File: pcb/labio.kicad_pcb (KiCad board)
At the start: 2 copper layers, 152 x 85 mm, 219 parts, among them IC201 dnp-AT24CS32-XHM, J701 JACK_TRRS_6PINS, P201 CONN_02X20, P301 CONN_01X04, P302 CONN_01X04, P303 CONN_01X04, P401 SFV12R-1ST__HLF, P601 CONN_01X02, P602 CONN_01X02, P603 CONN_01X04, P604 CONN_01X02, P605 CONN_01X03, P606 CONN_01X03, P607 CONN_01X05, P608 CONN_01X05, P701 CONN_01X04, P702 CONN_01X04, P703 CONN_01X04, P704 CONN_01X02, P901 CONN_01X06, Q301 PHOTOTRANSISTOR, Q302 Q_NMOS_GSD, Q303 Q_NMOS_GSD, Q601 Q_NMOS_GSD, Q602 Q_NMOS_GSD, Q603 Q_NMOS_GSD, Q604 Q_NMOS_GSD, Q605 Q_NMOS_GSD, Q606 Q_NMOS_GSD, Q607 Q_NMOS_GSD, Q608 Q_NMOS_GSD, Q609 Q_NMOS_GSD, Q610 Q_NMOS_GSD, Q611 Q_NMOS_GSD, Q612 Q_NMOS_GSD, Q613 Q_NMOS_GSD, SW301 DIP_SWITCH_X04, SW401 DIP_SWITCH_X04, SW501 DIP_SWITCH_X04, SW601 DIP_SWITCH_X04, SW602 DIP_SWITCH_X04, SW603 DIP_SWITCH_X04, SW604 DIP_SWITCH_X04, SW605 ROT_ENC, SW606 DIP_SWITCH_X04, SW701 DIP_SWITCH_X04, SW702 DIP_SWITCH_X04, SW801 SW_PUSH, SW802 SW_PUSH, SW803 SW_PUSH, SW804 SW_PUSH, SW805 SW_PUSH, U201 AP7365_SOT-23-5, U301 ADS1015, U501 LSM303D, U502 BMP280, U503 L3GD20H, U601 L298P_PowerSO20, U701 SPU0410HR5H, U702 WM8750

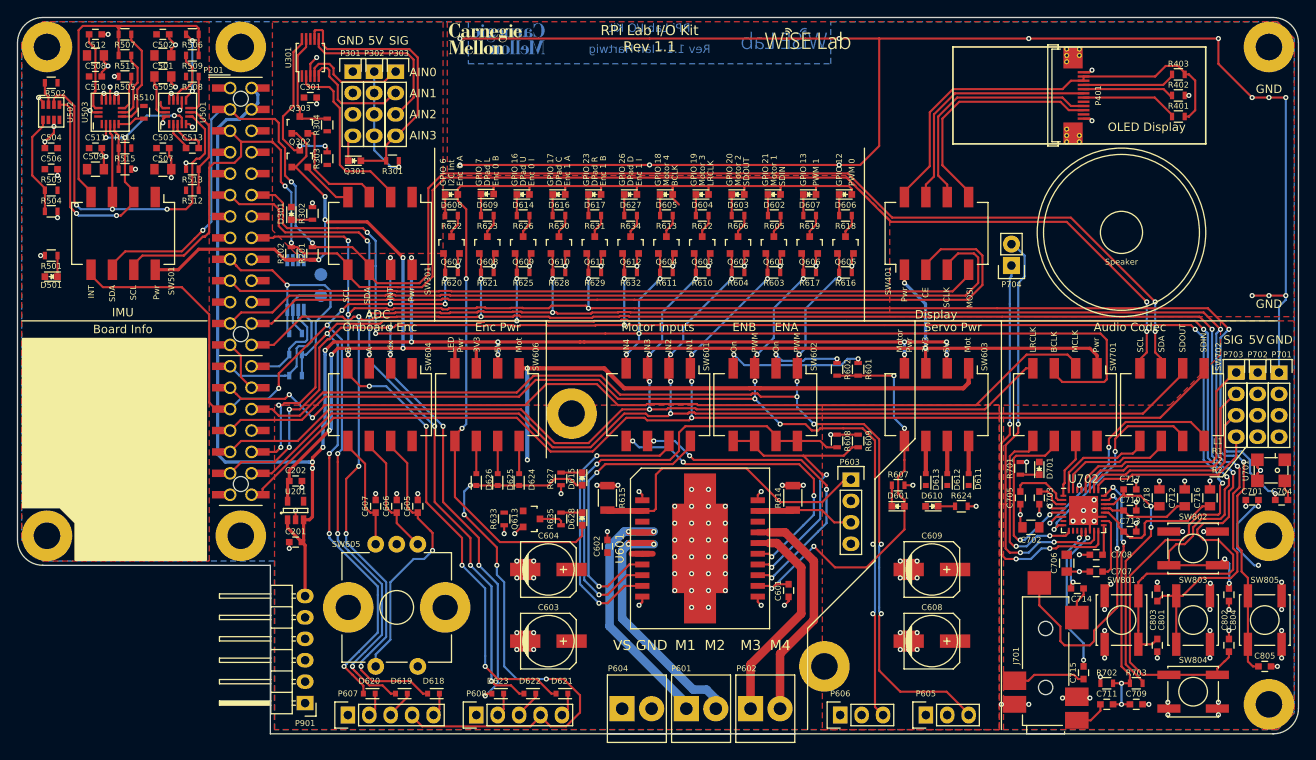
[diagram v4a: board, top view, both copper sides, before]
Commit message: add fuses for connectable headers (adc, encoder, motors, servo, codec). GERBER/BOM UPDATES ONLY
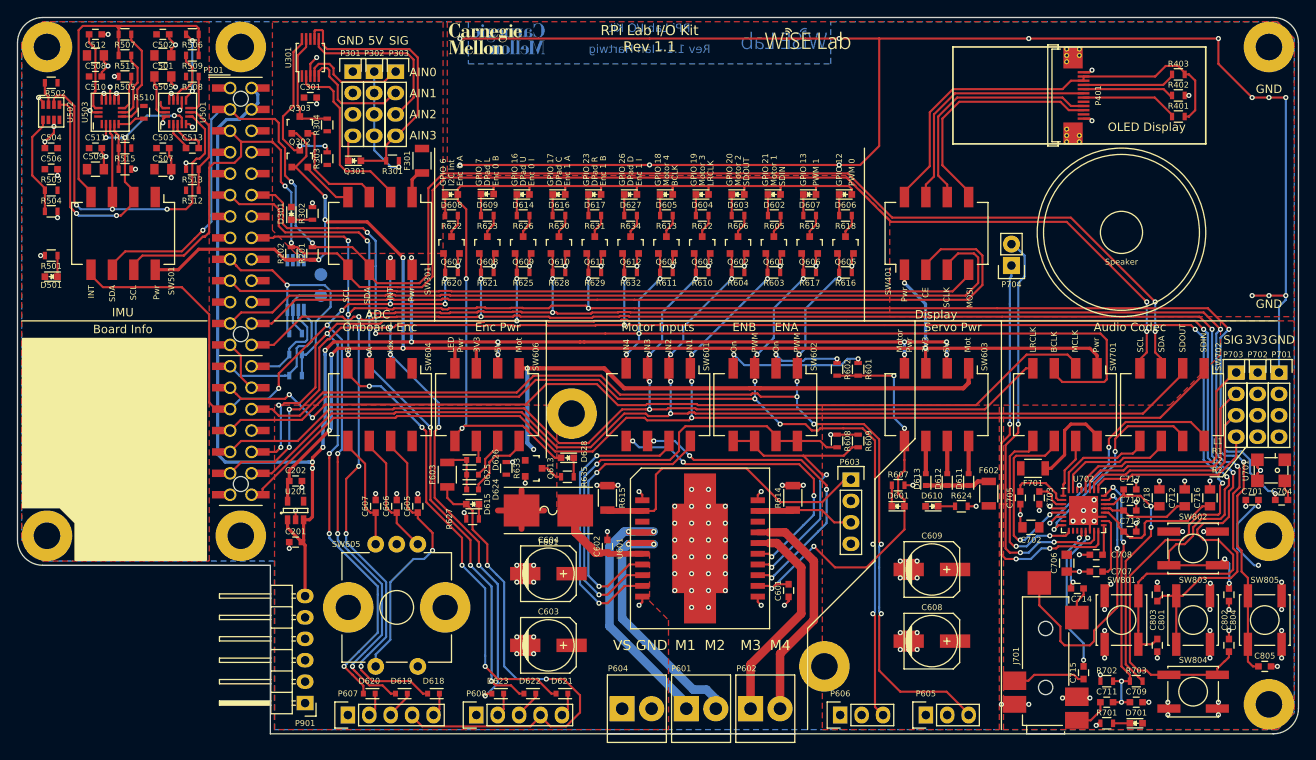
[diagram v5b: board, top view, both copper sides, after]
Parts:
- added F301: F_Small, Resistors_SMD:R_1206, F.Cu at (125.0, 67.0)
- added F601: F_Small, labio-special:OMNI-BLOCK_Fuse_10x5mm_Littelfuse, F.Cu at (140.0, 108.5)
- added F602: F_Small, Resistors_SMD:R_1206, F.Cu at (192.2, 106.5)
- added F603: F_Small, Resistors_SMD:R_1206, F.Cu at (128.0, 104.2)
- added F701: F_Small, Resistors_SMD:R_1206, F.Cu at (197.5, 103.5)
- moved D701 32.4 mm to (209.8, 133.8), turned to 0 degrees
- moved R701 31.9 mm to (206.2, 133.8), turned to 0 degrees
- moved D615 13.3 mm to (131.0, 107.8), turned to 180 degrees
- moved R627 11.5 mm to (131.0, 109.5), turned to 180 degrees
- moved D628 7.46 mm to (142.2, 102.2), turned to 180 degrees
- moved Q613 6.01 mm to (138.2, 103.5)
- moved R633 6.01 mm to (135.0, 103.5), turned to 90 degrees
- moved D624 5.65 mm to (131.0, 106.0), turned to 180 degrees
- moved R635 5.06 mm to (142.2, 104.5), turned to 180 degrees
- moved D625 3.04 mm to (131.0, 104.2), turned to 180 degrees
- moved D626 2.37 mm to (131.0, 102.5), turned to 180 degrees
- moved C603 0.50 mm to (140.0, 124.5)
- moved C604 0.50 mm to (140.0, 116.0)
- moved C709 0.25 mm to (209.8, 131.2)
- moved C711 0.25 mm to (206.2, 131.2)
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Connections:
- C602 pad 1: /labio-dio/VS_MOTOR -> /labio-dio/VS_MOTOR_F
- D611 pad 1: /labio-dio/VDD_SERVO -> /labio-dio/VDD_SERVO_F
- D612 pad 1: /labio-dio/VDD_SERVO -> /labio-dio/VDD_SERVO_F
- D613 pad 1: /labio-dio/VDD_SERVO -> /labio-dio/VDD_SERVO_F
- D624 pad 1: /labio-dio/VDD_ENC -> /labio-dio/VDD_ENC_F
- D625 pad 1: /labio-dio/VDD_ENC -> /labio-dio/VDD_ENC_F
- D626 pad 1: /labio-dio/VDD_ENC -> /labio-dio/VDD_ENC_F
- H1001 pad 1: Net-(H1001-Pad1) -> (no net)
- H1002 pad 1: Net-(H1002-Pad1) -> (no net)
- H1003 pad 1: Net-(H1003-Pad1) -> (no net)
- H1004 pad 1: Net-(H1004-Pad1) -> (no net)
- H1005 pad 1: Net-(H1005-Pad1) -> (no net)
- H1006 pad 1: Net-(H1006-Pad1) -> (no net)
- H1007 pad 1: Net-(H1007-Pad1) -> (no net)
- H1008 pad 1: Net-(H1008-Pad1) -> (no net)
- H1009 pad 1: Net-(H1009-Pad1) -> (no net)
- J701 pad 6: Net-(J701-Pad6) -> (no net)
- P401 pad 11: Net-(P401-Pad11) -> (no net)
- P401 pad 8: Net-(P401-Pad8) -> (no net)
- P901 pad 5: Net-(P901-Pad5) -> (no net)
- SW301 pad 1: /labio-adc/VDD5V_J -> /labio-adc/VDD_J_F
- SW604 pad 1: Net-(SW604-Pad1) -> (no net)
- SW604 pad 8: Net-(SW604-Pad8) -> (no net)
- SW701 pad 8: /labio-audio/VDD3V3_J -> /labio-audio/VDD3V3_J_F
- U601 pad 6: /labio-dio/VS_MOTOR -> /labio-dio/VS_MOTOR_F
- U702 pad 10: Net-(U702-Pad10) -> (no net)
- U702 pad 11: Net-(U702-Pad11) -> (no net)
- U702 pad 7: Net-(U702-Pad7) -> (no net)
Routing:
- net /labio-dio/VDD_LED: track 115.5 -> 102.1 mm
- net /labio-dio/VDD_ENC: track 72.5 -> 59.8 mm, vias 4 -> 2
- net /labio-dio/VS_MOTOR_F: track 0.00 -> 11.6 mm
- net /labio-audio/VDD3V3_J_F: track 0.00 -> 11.2 mm
- net /labio-dio/VDD_SERVO_F: track 0.00 -> 7.66 mm
- net /labio-dio/VS_MOTOR: track 69.7 -> 76.4 mm
- net /labio-dio/VDD_ENC_F: track 0.00 -> 5.92 mm
- net Net-(D624-Pad2): track 3.88 -> 8.74 mm
- net /labio-adc/VDD_J_F: track 0.00 -> 3.58 mm
- net Net-(J701-Pad6): track 3.25 -> 0.00 mm, vias 2 -> 0
- net (no net): track 0.00 -> 3.25 mm, vias 0 -> 2
- net GND: track 408.9 -> 407.4 mm
- net Net-(D626-Pad2): track 3.88 -> 2.36 mm
- net Net-(D625-Pad2): track 3.88 -> 4.95 mm
- net Net-(D615-Pad1): track 2.50 -> 1.75 mm

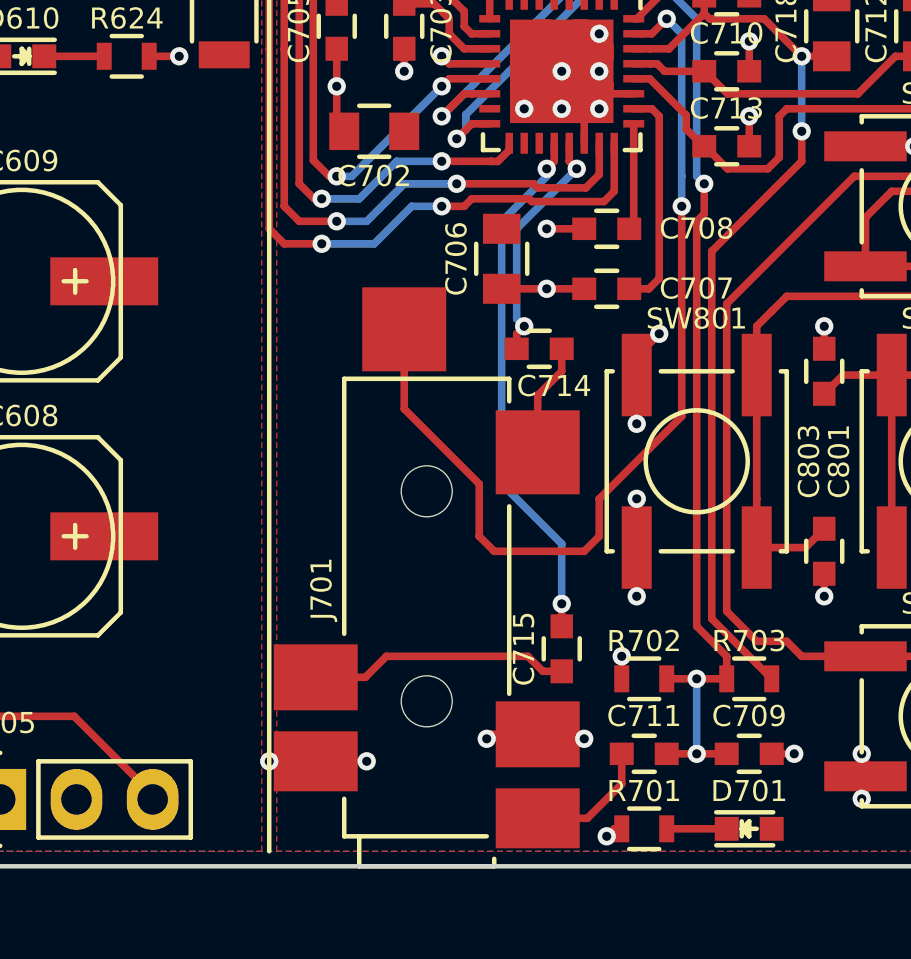
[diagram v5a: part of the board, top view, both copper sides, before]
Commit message: fix codec/mic/trrs bias circuit
* trrs (headset) mic bias was flipped (in vs out) from datasheet
* trrs l/r decoupling caps changed back to 220uF per datasheet and re-layout for 1210 ceramic
* mems mic decoupling changed to 1uF for consistency
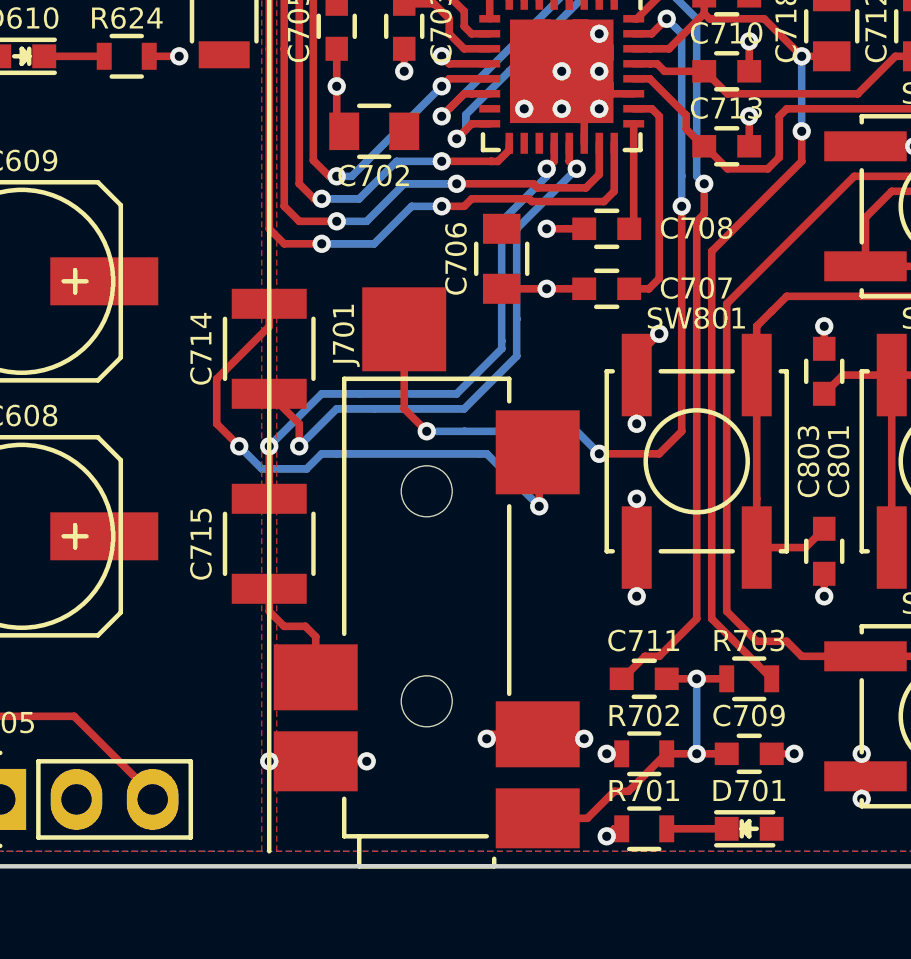
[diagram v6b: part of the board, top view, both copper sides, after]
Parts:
- C704: value 2.2uF -> 1uF
- C714, C715: value 220pF -> 220uF; footprint Capacitors_SMD:C_0603 -> Capacitors_SMD:C_1210
- moved C715 10.4 mm to (193.8, 124.2)
- moved C714 9.00 mm to (193.8, 117.8), turned to 270 degrees
- moved C711 2.50 mm to (206.2, 128.8), turned to 0 degrees
- moved R702 2.50 mm to (206.2, 131.2)
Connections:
- C709 pad 1: /labio-audio/TRRS_MIC_BIAS -> /labio-audio/TRRS_MIC_BIASED
- C711 pad 1: /labio-audio/TRRS_MIC_BIAS -> /labio-audio/TRRS_MIC
- C711 pad 2: /labio-audio/TRRS_MIC -> /labio-audio/TRRS_MIC_BIASED
- J701 pad 1: /labio-audio/TRRS_MIC -> /labio-audio/TRRS_MIC_BIASED
- R702 pad 1: /labio-audio/TRRS_MIC_BIAS -> /labio-audio/TRRS_MIC_BIASED
- R703 pad 2: /labio-audio/TRRS_MIC_BIAS -> /labio-audio/TRRS_MIC_BIASED
- U702 pad 24: /labio-audio/TRRS_MIC_BIAS -> /labio-audio/TRRS_MIC
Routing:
- net /labio-audio/TRRS_MIC_BIAS: track 32.0 -> 0.00 mm, vias 4 -> 0
- net /labio-audio/TRRS_MIC: track 4.28 -> 26.5 mm, vias 0 -> 2
- net /labio-audio/TRRS_L: track 3.78 -> 18.8 mm, vias 0 -> 2
- net /labio-audio/TRRS_MIC_BIASED: track 0.00 -> 11.7 mm, vias 0 -> 2
- net /labio-audio/TRRS_L_C: track 7.99 -> 18.7 mm
- net /labio-audio/TRRS_R: track 8.70 -> 4.01 mm
- net /labio-audio/TRRS_HPDETECT: track 31.3 -> 28.1 mm, vias 2 -> 4
- net /labio-audio/TRRS_R_C: track 17.7 -> 18.4 mm

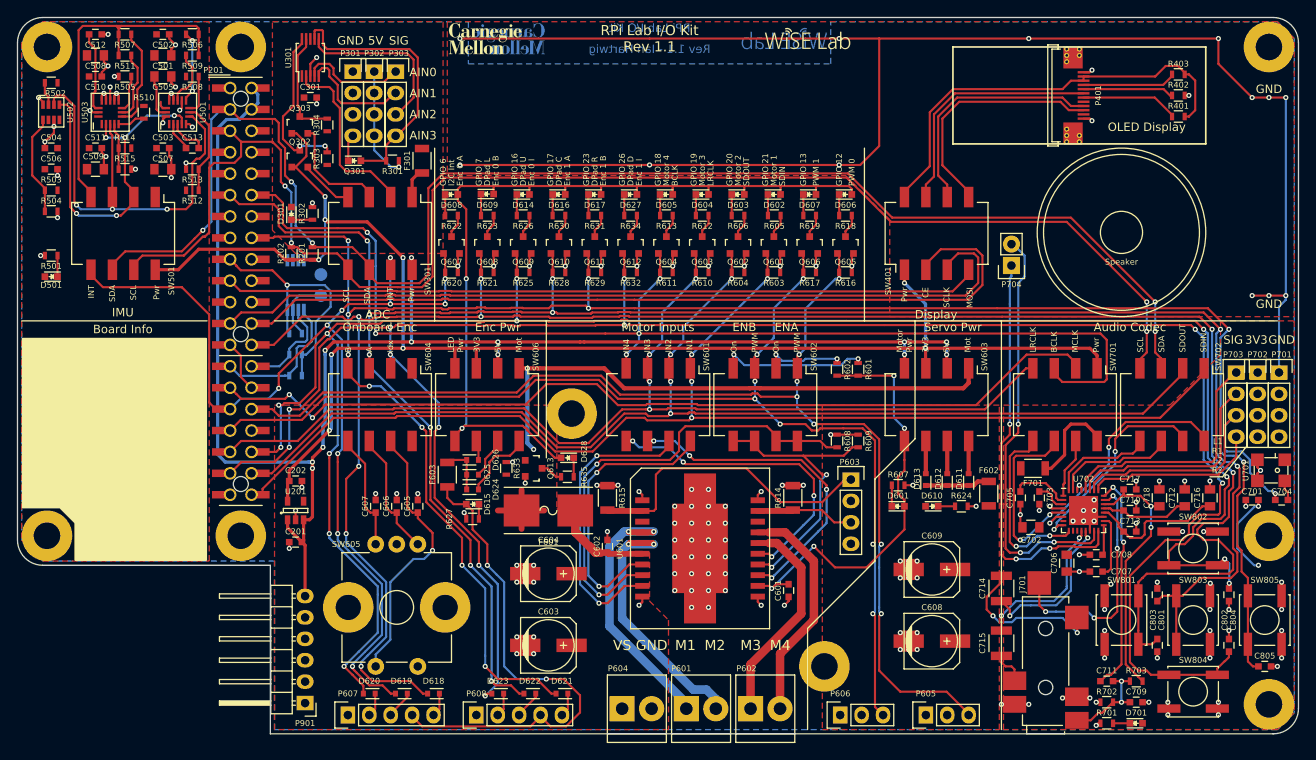
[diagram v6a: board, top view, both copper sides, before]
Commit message: Fix ADC reading mic, possible backpowering, encoder pull downs, vias in footprint:
* Mic needs on-board path to ADC. Add proper bias and amp. Connect to ADC or codec with switches.
* Mic footprint (U701) flipped. Redraw footprint and adjust routing.
* Remove power from dip switches and replace with fuses. Turning power off to a block could result in backpower from driven IO lines.
* Remove/adjust pull downs on LEDs for encoder/dpad lines.
* Move vias out of display connector (P401) footprint.
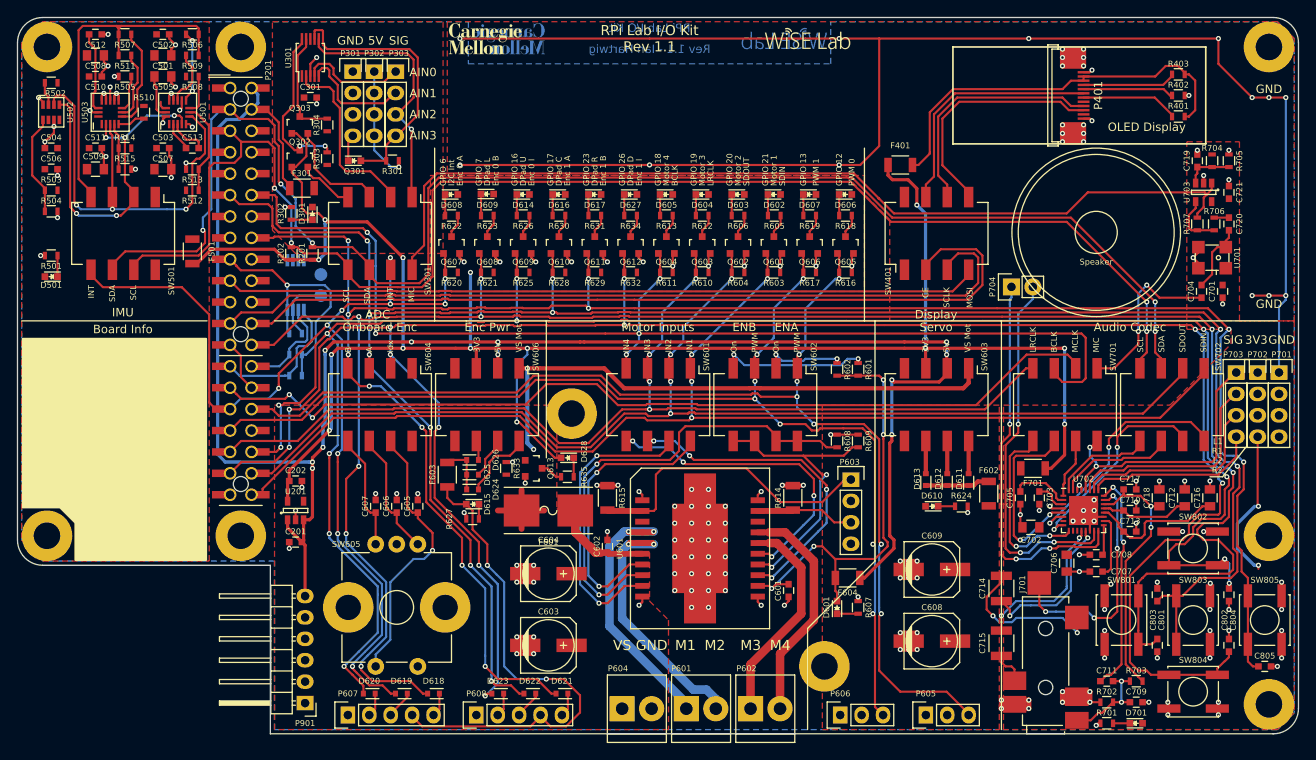
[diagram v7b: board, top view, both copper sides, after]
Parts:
- added C719: 1uF, Capacitors_SMD:C_0603, F.Cu at (217.0, 67.0)
- added C720: 1uF, Capacitors_SMD:C_0603, F.Cu at (220.8, 74.5)
- added C721: 0.1uF, Capacitors_SMD:C_0603, F.Cu at (220.8, 70.8)
- added F401: F_Small, Resistors_SMD:R_1206, F.Cu at (181.8, 67.5)
- added F501: F_Small, Resistors_SMD:R_1206, F.Cu at (97.8, 77.8)
- added F604: F_Small, Resistors_SMD:R_1206, F.Cu at (175.5, 116.5)
- added R704: 10k, Resistors_SMD:R_0603, F.Cu at (218.8, 67.0)
- added R705: 10k, Resistors_SMD:R_0603, F.Cu at (220.8, 67.0)
- added R706: 10k, Resistors_SMD:R_0603, F.Cu at (219.0, 74.5)
- added R707: 820k, Resistors_SMD:R_0603, F.Cu at (217.0, 74.5)
- added U703: OPA344_SOT23-5, TO_SOT_Packages_SMD:SOT-23-5, F.Cu at (217.8, 70.8)
- moved C704 26.5 mm to (217.5, 82.5), turned to 90 degrees
- moved U701 26.2 mm to (218.8, 78.5)
- moved C701 25.0 mm to (220.0, 82.5), turned to 90 degrees
- moved R607 15.3 mm to (176.8, 120.0), turned to 90 degrees
- moved F301 14.6 mm to (110.8, 70.2), turned to 180 degrees
- moved D601 14.0 mm to (174.2, 120.0), turned to 90 degrees
- moved P704 2.54 mm to (194.9, 82.0), turned to 90 degrees
- moved D301 2.50 mm to (112.0, 73.2)
- moved R302 2.50 mm to (109.5, 73.2)
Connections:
- net /labio-adc/ACD_AIN0 renamed /labio-adc/ADC_AIN0
- C704 pad 1: /labio-audio/LINPUT2 -> /labio-audio/MEMS_MIC_C
- D602 pad 2: /labio-dio/VDD_LED -> /3V3_EXTRA
- D603 pad 2: /labio-dio/VDD_LED -> /3V3_EXTRA
- D604 pad 2: /labio-dio/VDD_LED -> /3V3_EXTRA
- D605 pad 2: /labio-dio/VDD_LED -> /3V3_EXTRA
- D606 pad 2: /labio-dio/VDD_LED -> /3V3_EXTRA
- D607 pad 2: /labio-dio/VDD_LED -> /3V3_EXTRA
- D608 pad 2: /labio-dio/VDD_LED -> /3V3_EXTRA
- D609 pad 2: /labio-dio/VDD_LED -> /3V3_EXTRA
- D614 pad 2: /labio-dio/VDD_LED -> /3V3_EXTRA
- D616 pad 2: /labio-dio/VDD_LED -> /3V3_EXTRA
- D617 pad 2: /labio-dio/VDD_LED -> /3V3_EXTRA
- D627 pad 2: /labio-dio/VDD_LED -> /3V3_EXTRA
- D628 pad 2: /labio-dio/VDD_LED -> /3V3_EXTRA
- F301 pad 2: /labio-adc/VDD_J_F -> /5V
- F701 pad 1: /labio-audio/VDD3V3_J_F -> /3V3_EXTRA
- P401 pad 2: Net-(P401-Pad2) -> Net-(F401-Pad2)
- P401 pad 3: Net-(P401-Pad2) -> Net-(F401-Pad2)
- R401 pad 2: Net-(P401-Pad2) -> Net-(F401-Pad2)
- R403 pad 2: Net-(P401-Pad2) -> Net-(F401-Pad2)
- R607 pad 1: GND -> Net-(D601-Pad1)
- R607 pad 2: Net-(D601-Pad1) -> GND
- R620 pad 2: GND -> /3V3_EXTRA
- R621 pad 2: GND -> /3V3_EXTRA
- R625 pad 2: GND -> /3V3_EXTRA
- R628 pad 2: GND -> /3V3_EXTRA
- R629 pad 2: GND -> /3V3_EXTRA
- R632 pad 2: GND -> /3V3_EXTRA
- SW301 pad 1: /labio-adc/VDD_J_F -> /labio-adc/ADC_AIN2
- SW301 pad 8: /5V -> MEMS_MIC_TO_ADC
- SW401 pad 1: /3V3_EXTRA -> (no net)
- SW401 pad 8: Net-(P401-Pad2) -> (no net)
- SW501 pad 1: /labio-imu/VDD3V3_J -> (no net)
- SW501 pad 8: /3V3_EXTRA -> (no net)
- SW603 pad 4: /5V -> (no net)
- SW603 pad 5: /labio-dio/VDD_MOT -> (no net)
- SW606 pad 4: /3V3_EXTRA -> (no net)
- SW606 pad 5: /labio-dio/VDD_LED -> (no net)
- SW701 pad 1: /3V3_EXTRA -> /labio-audio/MEMS_MIC_C
- SW701 pad 8: /labio-audio/VDD3V3_J_F -> /labio-audio/LINPUT1
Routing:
- net MEMS_MIC_TO_ADC: track 0.00 -> 112.0 mm
- net /labio-dio/VDD_LED: track 102.1 -> 0.00 mm, vias 2 -> 0
- net Net-(P401-Pad2): track 51.3 -> 0.00 mm
- net Net-(F401-Pad2): track 0.00 -> 47.5 mm
- net /3V3_EXTRA: track 191.8 -> 235.2 mm, vias 9 -> 14
- net (no net): track 3.25 -> 35.2 mm, vias 2 -> 16
- net /5V: track 191.1 -> 220.9 mm, vias 12 -> 11
- net /labio-audio/MEMS_MIC_C: track 0.00 -> 20.6 mm, vias 0 -> 2
- net /labio-audio/LINPUT2: track 38.1 -> 23.6 mm, vias 1 -> 0
- net /labio-audio/VDD3V3_J_F: track 11.2 -> 0.00 mm
- net /labio-adc/ADC_AIN2: track 20.3 -> 31.0 mm, vias 0 -> 1
- net /labio-audio/VDD3V3_J: track 32.3 -> 40.3 mm
- net Net-(R706-Pad2): track 0.00 -> 6.56 mm
- net /labio-audio/MEMS_MIC: track 2.42 -> 8.43 mm
- net GND: track 407.1 -> 413.0 mm, vias 176 -> 181
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- added copper zone on F.Cu, net /3V3_EXTRA
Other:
- board text added: "MIC"
- board text added: "Servo"
- board text added: "VS Mot"
- board text removed: "LED Pwr"
- board text removed: "Mot"
- board text removed: "Motor Pwr"
- board text removed: "Pwr"
- board text removed: "Servo Pwr"
